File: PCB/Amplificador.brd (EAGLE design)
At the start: 102.5 x 80 mm, 36 parts, among them Q1 BC214, Q10 MJE2955, Q11 MJE3055, Q2 BC214, Q3 BC214, Q4 BC214, Q5 2N3904, Q6 2N3904, Q7 2N3904, Q8 2N3904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

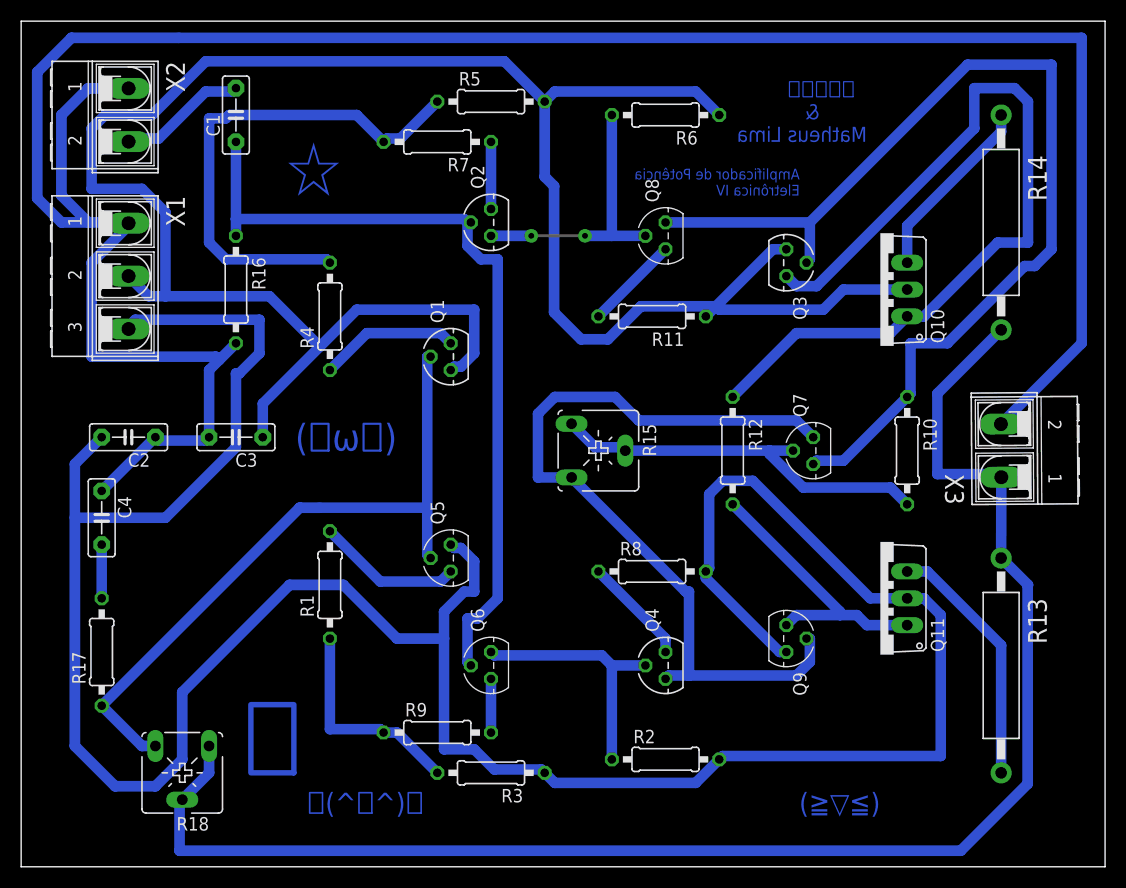
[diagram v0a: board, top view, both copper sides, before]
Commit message: Placa Versão 2.0
Talvez a versão final, compatível com nossos componentes comprados
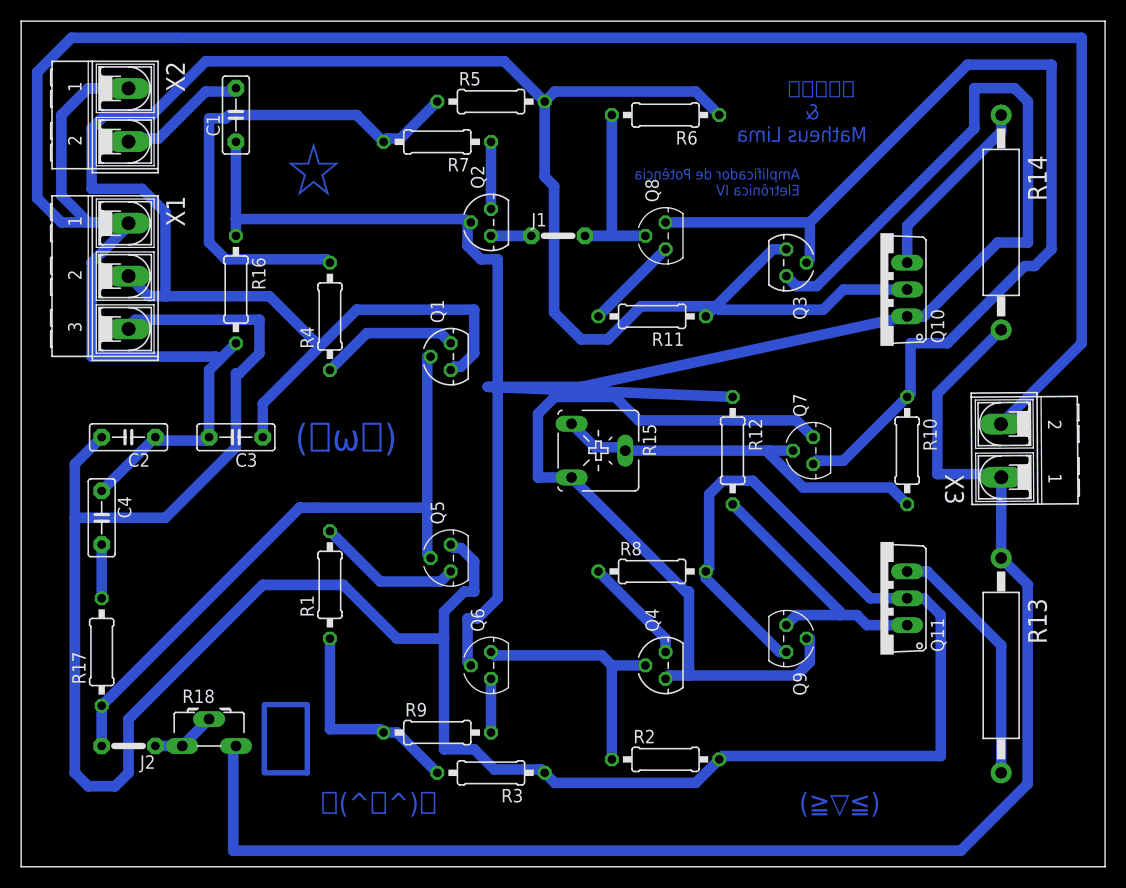
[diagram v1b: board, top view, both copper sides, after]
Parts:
- added J1, J2: J5MM, jumper:05
- R18: device pot:CA6V -> pot:CA6H
- moved R18 3.59 mm to (15.2, 11.4), turned to 0 degrees
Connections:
- new net N$25: J1.1, Q2.3, R6.2
- new net N$26: J2.1, Q1.2, Q5.2, R17.1
- net N$15: now also R18.E; no longer R18.A, R18.S
- net N$19: now also J2.2, R18.A, R18.S; no longer Q1.2, Q5.2, R17.1, R18.E
- net N$2: now also J1.2; no longer Q2.3, R6.2
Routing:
- net N$26: track 0.00 -> 68.0 mm
- net N$19: track 64.7 -> 0.00 mm
- net N$3: track 81.1 -> 125.0 mm
- net N$25: track 0.00 -> 15.2 mm
- net N$2: track 18.4 -> 5.72 mm
- net N$15: track 146.3 -> 140.2 mm
- net N$20: track 5.08 -> 0.00 mm, vias 1 -> 0
- net N$22: track 2.54 -> 0.00 mm, vias 1 -> 0
- net V+: track 255.9 -> 256.7 mm
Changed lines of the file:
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@@
 Eletrônica IV</text>
 <text x="33.02" y="39.37" size="2.54" layer="16" rot="MR0">(･ω･)</text>
-<text x="24.13" y="8.89" size="6.4516" layer="16" rot="MR0">𝄞</text>
+<text x="25.4" y="8.89" size="6.4516" layer="16" rot="MR0">𝄞</text>
 <text x="27.94" y="63.5" size="5.08" layer="16" rot="MR0">☆</text>
 <text x="78.74" y="5.08" size="1.9304" layer="16" rot="MR0">(≧▽≦)</text>
-<text x="35.56" y="5.08" size="1.9304" layer="16" rot="MR0">ヽ(^。^)ノ</text>
+<text x="36.83" y="5.08" size="1.9304" layer="16" rot="MR0">ヽ(^。^)ノ</text>
 </plain>
 <attributes>
@@
 <element name="R16" library="resistor" library_urn="urn:adsk.eagle:library:348" package="0207/10" package3d_urn="urn:adsk.eagle:package:25939/1" value="47k" x="17.78" y="54.61" rot="R270"/>
 <element name="R17" library="resistor" library_urn="urn:adsk.eagle:library:348" package="0207/10" package3d_urn="urn:adsk.eagle:package:25939/1" value="2.2k" x="5.08" y="20.32" rot="R90"/>
-<element name="R18" library="pot" library_urn="urn:adsk.eagle:library:331" package="CA6V" package3d_urn="urn:adsk.eagle:package:22691/1" value="47k" x="12.7" y="8.89" rot="R180"/>
 <element name="R2" library="resistor" library_urn="urn:adsk.eagle:library:348" package="0207/10" package3d_urn="urn:adsk.eagle:package:25939/1" value="2.55k" x="58.42" y="10.16"/>
 <element name="R3" library="resistor" library_urn="urn:adsk.eagle:library:348" package="0207/10" package3d_urn="urn:adsk.eagle:package:25939/1" value="8.66k" x="41.91" y="8.89" rot="R180"/>
@@
 <element name="Q10" library="transistor-power" library_urn="urn:adsk.eagle:library:400" package="TO220AV" package3d_urn="urn:adsk.eagle:package:29487/1" value="MJE2955" x="78.74" y="54.61" rot="R90"/>
 <element name="Q11" library="transistor-power" library_urn="urn:adsk.eagle:library:400" package="TO220AV" package3d_urn="urn:adsk.eagle:package:29487/1" value="MJE3055" x="78.74" y="25.4" rot="R90"/>
+<element name="J1" library="jumper" library_urn="urn:adsk.eagle:library:252" package="05" package3d_urn="urn:adsk.eagle:package:15465/1" value="J5MM" x="48.26" y="59.69"/>
+<element name="R18" library="pot" library_urn="urn:adsk.eagle:library:331" package="CA6H" package3d_urn="urn:adsk.eagle:package:22689/1" value="47k" x="15.24" y="11.43"/>
+<element name="J2" library="jumper" library_urn="urn:adsk.eagle:library:252" package="05" package3d_urn="urn:adsk.eagle:package:15465/1" value="J5MM" x="7.62" y="11.43" rot="R180"/>
 </elements>
 <signals>
 <signal name="N$2">
-<contactref element="R6" pad="2"/>
-<contactref element="Q2" pad="3"/>
 <contactref element="Q8" pad="2"/>
-<wire x1="56.515" y1="59.69" x2="53.34" y2="59.69" width="1" layer="16"/>
-<wire x1="53.34" y1="59.69" x2="53.34" y2="71.12" width="1" layer="16"/>
-<wire x1="41.91" y1="59.69" x2="45.72" y2="59.69" width="1.016" layer="16"/>
-<wire x1="45.72" y1="59.69" x2="53.34" y2="59.69" width="0" layer="19" extent="16-16"/>
+<contactref element="J1" pad="2"/>
+<wire x1="50.8" y1="59.69" x2="56.515" y2="59.69" width="1.016" layer="16"/>
 </signal>
 <signal name="N$3">
@@
 <contactref element="Q3" pad="1"/>
 <contactref element="Q10" pad="B"/>
-<wire x1="70.8025" y1="50.4825" x2="64.77" y2="44.45" width="1" layer="16"/>
-<wire x1="79.6925" y1="50.4825" x2="70.8025" y2="50.4825" width="1" layer="16"/>
-<wire x1="81.28" y1="52.07" x2="79.6925" y2="50.4825" width="1" layer="16"/>
+<wire x1="41.5925" y1="45.4025" x2="64.77" y2="44.45" width="1" layer="16"/>
+<wire x1="50.4825" y1="45.4025" x2="41.5925" y2="45.4025" width="1" layer="16"/>
+<wire x1="81.28" y1="52.07" x2="50.4825" y2="45.4025" width="1" layer="16"/>
 <wire x1="70.8025" y1="54.9275" x2="69.85" y2="55.88" width="1" layer="16"/>
 <wire x1="72.7075" y1="54.9275" x2="70.8025" y2="54.9275" width="1" layer="16"/>
@@
 <contactref element="R14" pad="2"/>
 <contactref element="X3" pad="1"/>
-<contactref element="R18" pad="A"/>
-<contactref element="R18" pad="S"/>
 <wire x1="90.17" y1="29.21" x2="90.187553125" y2="36.855459375" width="1" layer="16"/>
 <wire x1="84.1375" y1="44.7675" x2="90.17" y2="50.8" width="1" layer="16"/>
@@
 <wire x1="89.8525" y1="37.1475" x2="84.1375" y2="37.1475" width="1" layer="16"/>
 <wire x1="89.8525" y1="37.1475" x2="90.187553125" y2="36.855459375" width="1" layer="16"/>
-<wire x1="86.35085" y1="1.524" x2="12.446" y2="1.524" width="1.016" layer="16"/>
+<wire x1="86.35085" y1="1.524" x2="17.526" y2="1.524" width="1.016" layer="16"/>
 <wire x1="86.35085" y1="1.524" x2="92.678" y2="7.85115" width="1.016" layer="16"/>
 <wire x1="92.71" y1="26.67" x2="90.17" y2="29.21" width="1.016" layer="16"/>
 <wire x1="92.678" y1="7.85115" x2="92.678" y2="26.638" width="1.016" layer="16"/>
 <wire x1="92.678" y1="26.638" x2="92.71" y2="26.67" width="1.016" layer="16"/>
-<wire x1="15.24" y1="11.43" x2="15.24" y2="8.89" width="1.016" layer="16"/>
-<wire x1="12.7" y1="6.35" x2="15.24" y2="8.89" width="1.016" layer="16"/>
-<wire x1="12.446" y1="6.096" x2="12.7" y2="6.35" width="1.016" layer="16"/>
-<wire x1="12.446" y1="1.524" x2="12.446" y2="6.096" width="1.016" layer="16"/>
+<contactref element="R18" pad="E"/>
+<wire x1="17.526" y1="11.176" x2="17.78" y2="11.43" width="1.016" layer="16"/>
+<wire x1="17.526" y1="1.524" x2="17.526" y2="11.176" width="1.016" layer="16"/>
 </signal>
 <signal name="N$16">
@@
 <wire x1="63.8175" y1="10.4775" x2="84.455" y2="10.4775" width="1" layer="16"/>
 <wire x1="63.8175" y1="10.4775" x2="63.5" y2="10.16" width="1" layer="16"/>
-<wire x1="2.54" y1="33.02" x2="2.54" y2="11.43" width="1.016" layer="16"/>
-<wire x1="2.54" y1="11.43" x2="6.35" y2="7.62" width="1.016" layer="16"/>
-<wire x1="6.35" y1="7.62" x2="10.16" y2="7.62" width="1.016" layer="16"/>
-<wire x1="12.7" y1="16.51" x2="22.86" y2="26.67" width="1.016" layer="16"/>
-<wire x1="22.86" y1="26.67" x2="27.94" y2="26.67" width="1.016" layer="16"/>
 <wire x1="27.94" y1="26.67" x2="33.02" y2="21.59" width="1.016" layer="16"/>
 <wire x1="33.02" y1="21.59" x2="37.465" y2="21.59" width="1.016" layer="16"/>
-<wire x1="12.7" y1="10.16" x2="12.7" y2="16.51" width="1.016" layer="16"/>
-<wire x1="10.16" y1="7.62" x2="12.7" y2="10.16" width="1.016" layer="16"/>
+<wire x1="2.54" y1="8.89" x2="3.81" y2="7.62" width="1.016" layer="16"/>
+<wire x1="3.81" y1="7.62" x2="6.35" y2="7.62" width="1.016" layer="16"/>
+<wire x1="6.35" y1="7.62" x2="7.62" y2="8.89" width="1.016" layer="16"/>
+<wire x1="7.62" y1="8.89" x2="7.62" y2="13.97" width="1.016" layer="16"/>
+<wire x1="2.54" y1="33.02" x2="2.54" y2="8.89" width="1.016" layer="16"/>
+<wire x1="7.62" y1="13.97" x2="20.32" y2="26.67" width="1.016" layer="16"/>
+<wire x1="20.32" y1="26.67" x2="27.94" y2="26.67" width="1.016" layer="16"/>
 </signal>
 <signal name="V-">
@@
 <wire x1="5.08" y1="30.48" x2="5.08" y2="25.4" width="1" layer="16"/>
 </signal>
-<signal name="N$19">
+<signal name="N$20">
+<wire x1="45.72" y1="59.69" x2="50.8" y2="59.69" width="0" layer="19" extent="1-16"/>
+</signal>
+<signal name="N$22">
+<wire x1="50.8" y1="59.69" x2="53.34" y2="59.69" width="0" layer="19" extent="1-16"/>
+</signal>
+<signal name="N$25">
+<contactref element="R6" pad="2"/>
+<contactref element="Q2" pad="3"/>
+<contactref element="J1" pad="1"/>
+<wire x1="41.91" y1="59.69" x2="45.72" y2="59.69" width="1.016" layer="16"/>
+<wire x1="53.34" y1="71.12" x2="53.34" y2="59.69" width="1.016" layer="16"/>
+<wire x1="45.72" y1="59.69" x2="53.34" y2="59.69" width="0" layer="19" extent="16-16"/>
+</signal>
+<signal name="N$26">
 <contactref element="Q1" pad="2"/>
 <contactref element="Q5" pad="2"/>
-<contactref element="R18" pad="E"/>
 <contactref element="R17" pad="1"/>
 <wire x1="35.8775" y1="29.5275" x2="36.195" y2="29.21" width="1" layer="16"/>
@@
 <wire x1="35.8775" y1="33.9725" x2="25.7175" y2="33.9725" width="1" layer="16"/>
 <wire x1="25.7175" y1="33.9725" x2="23.8125" y2="33.9725" width="1.016" layer="16"/>
-<wire x1="5.08" y1="15.24" x2="23.8125" y2="33.9725" width="1.016" layer="16"/>
-<wire x1="10.16" y1="11.43" x2="8.89" y2="11.43" width="1.016" layer="16"/>
-<wire x1="8.89" y1="11.43" x2="5.08" y2="15.24" width="1.016" layer="16"/>
-</signal>
-<signal name="N$20">
-<via x="45.72" y="59.69" extent="1-16" drill="0.55" diameter="1.3" shape="octagon"/>
-<wire x1="45.72" y1="59.69" x2="50.8" y2="59.69" width="0.254" layer="1"/>
-</signal>
-<signal name="N$22">
-<via x="50.8" y="59.69" extent="1-16" drill="0.55" diameter="1.3" shape="octagon"/>
-<wire x1="50.8" y1="59.69" x2="53.34" y2="59.69" width="1.016" layer="16"/>
+<wire x1="23.8125" y1="33.9725" x2="5.08" y2="15.24" width="1.016" layer="16"/>
+<contactref element="J2" pad="1"/>
+<wire x1="5.08" y1="15.24" x2="5.08" y2="11.43" width="1.016" layer="16"/>
+<wire x1="10.16" y1="11.43" x2="12.7" y2="11.43" width="1.016" layer="16"/>
+<wire x1="12.7" y1="11.43" x2="15.24" y2="13.97" width="1.016" layer="16"/>
+<wire x1="5.08" y1="11.43" x2="10.16" y2="11.43" width="0" layer="19" extent="16-16"/>
+</signal>
+<signal name="N$19">
+<contactref element="R18" pad="S"/>
+<contactref element="R18" pad="A"/>
+<contactref element="J2" pad="2"/>
+<wire x1="12.7" y1="11.43" x2="15.24" y2="13.97" width="0" layer="19" extent="1-1"/>
+<wire x1="5.08" y1="11.43" x2="12.7" y2="11.43" width="0" layer="19" extent="1-1"/>
 </signal>
 </signals>

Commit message: Trabalho de eletrônica versão 2.1
Agora sim talvez a versão final, a anterior estava com erro
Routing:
- net N$3: track 125.0 -> 82.6 mm
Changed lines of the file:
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@@
 <contactref element="Q3" pad="1"/>
 <contactref element="Q10" pad="B"/>
-<wire x1="41.5925" y1="45.4025" x2="64.77" y2="44.45" width="1" layer="16"/>
-<wire x1="50.4825" y1="45.4025" x2="41.5925" y2="45.4025" width="1" layer="16"/>
-<wire x1="81.28" y1="52.07" x2="50.4825" y2="45.4025" width="1" layer="16"/>
 <wire x1="70.8025" y1="54.9275" x2="69.85" y2="55.88" width="1" layer="16"/>
 <wire x1="72.7075" y1="54.9275" x2="70.8025" y2="54.9275" width="1" layer="16"/>
@@
 <wire x1="82.8675" y1="52.07" x2="89.8525" y2="59.055" width="1" layer="16"/>
 <wire x1="81.28" y1="52.07" x2="82.8675" y2="52.07" width="1" layer="16"/>
+<wire x1="64.77" y1="44.45" x2="64.77" y2="46.99" width="1.016" layer="16"/>
+<wire x1="64.77" y1="46.99" x2="67.31" y2="49.53" width="1.016" layer="16"/>
+<wire x1="67.31" y1="49.53" x2="78.74" y2="49.53" width="1.016" layer="16"/>
+<wire x1="78.74" y1="49.53" x2="81.28" y2="52.07" width="1.016" layer="16"/>
 </signal>
 <signal name="N$6">
